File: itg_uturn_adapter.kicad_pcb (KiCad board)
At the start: 2 copper layers, 21.6 x 59.7 mm, 2 parts, among them J1 PinSocket_02x20, J2 BoxHeader_02x20

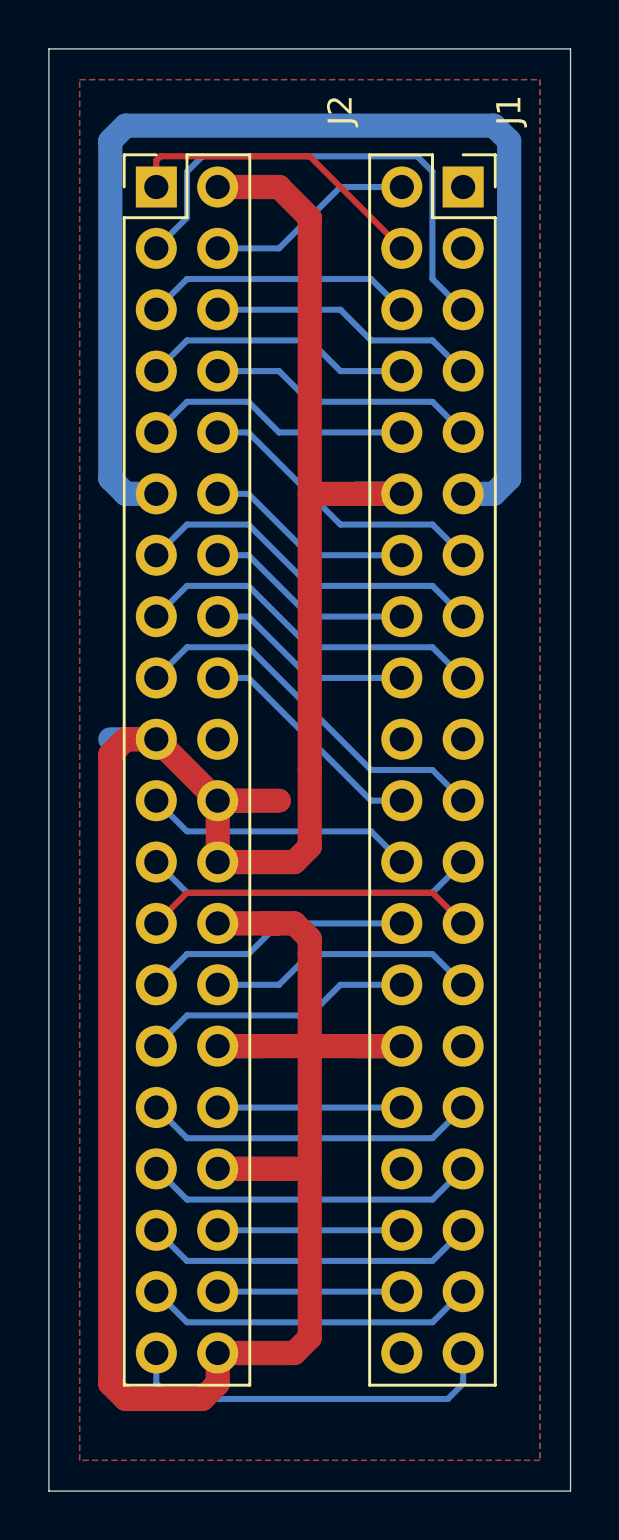
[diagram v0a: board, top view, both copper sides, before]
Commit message: modified external forms
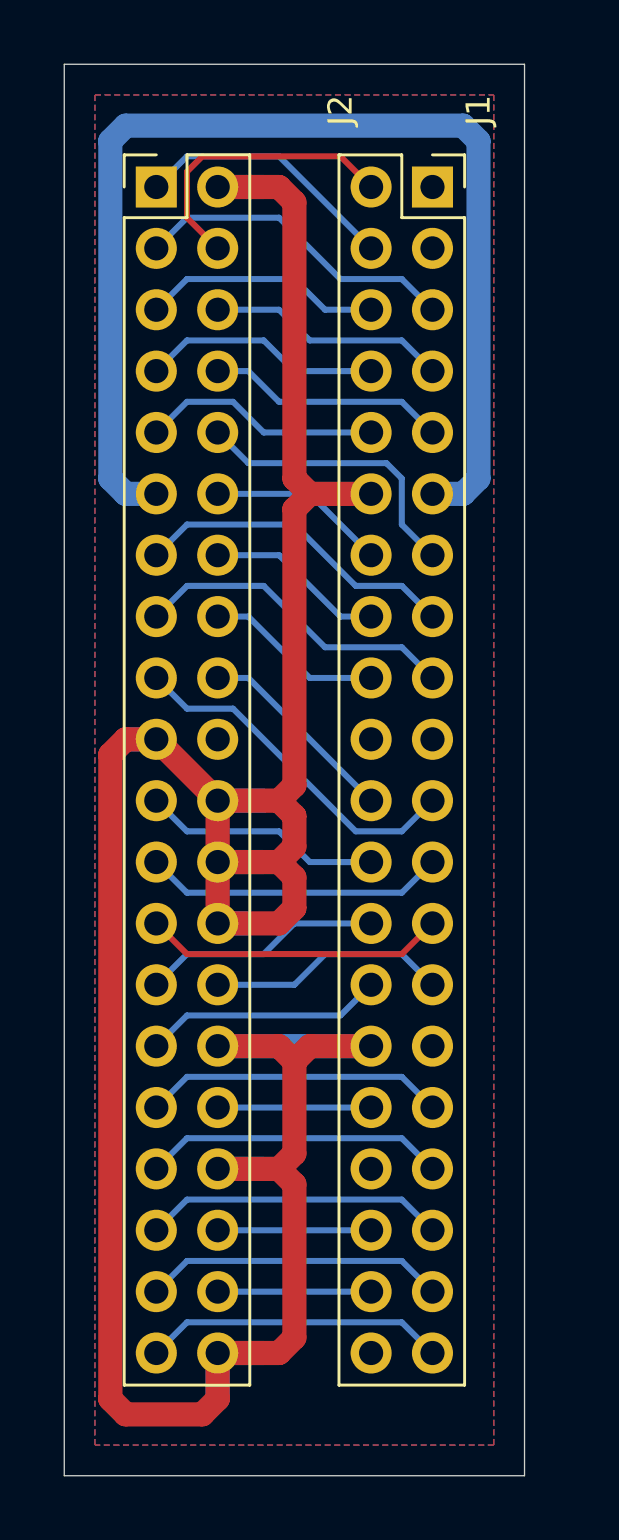
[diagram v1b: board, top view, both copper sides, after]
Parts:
- moved J1 1.27 mm to (102.9, 64.8)
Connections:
- net Net-(J1-Pad11) renamed +5V
- net Net-(J1-Pad12) renamed GND
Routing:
- net GND: track 183.7 -> 134.7 mm
- net Net-(J1-Pad5): track 20.6 -> 13.5 mm
- net Net-(J1-Pad2): track 8.67 -> 12.1 mm
- net Net-(J1-Pad39): track 15.8 -> 12.5 mm
- net Net-(J1-Pad4): track 12.9 -> 11.0 mm
- net Net-(J1-Pad37): track 13.8 -> 12.5 mm
- net Net-(J1-Pad33): track 13.8 -> 12.5 mm
- net Net-(J1-Pad21): track 15.9 -> 14.6 mm
- net Net-(J1-Pad7): track 11.2 -> 9.94 mm
- net Net-(J1-Pad10): track 11.2 -> 9.94 mm
- net Net-(J1-Pad35): track 13.8 -> 12.5 mm
- net Net-(J1-Pad25): track 13.8 -> 12.5 mm
- net Net-(J1-Pad23): track 13.8 -> 12.5 mm
- net Net-(J1-Pad9): track 11.2 -> 9.94 mm
- net Net-(J1-Pad8): track 11.2 -> 9.94 mm
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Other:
- board size 21.6 x 59.7 mm -> 19.1 x 58.4 mm
- rule trace_min: 0.2 -> 0.25

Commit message: add some vias to gnd
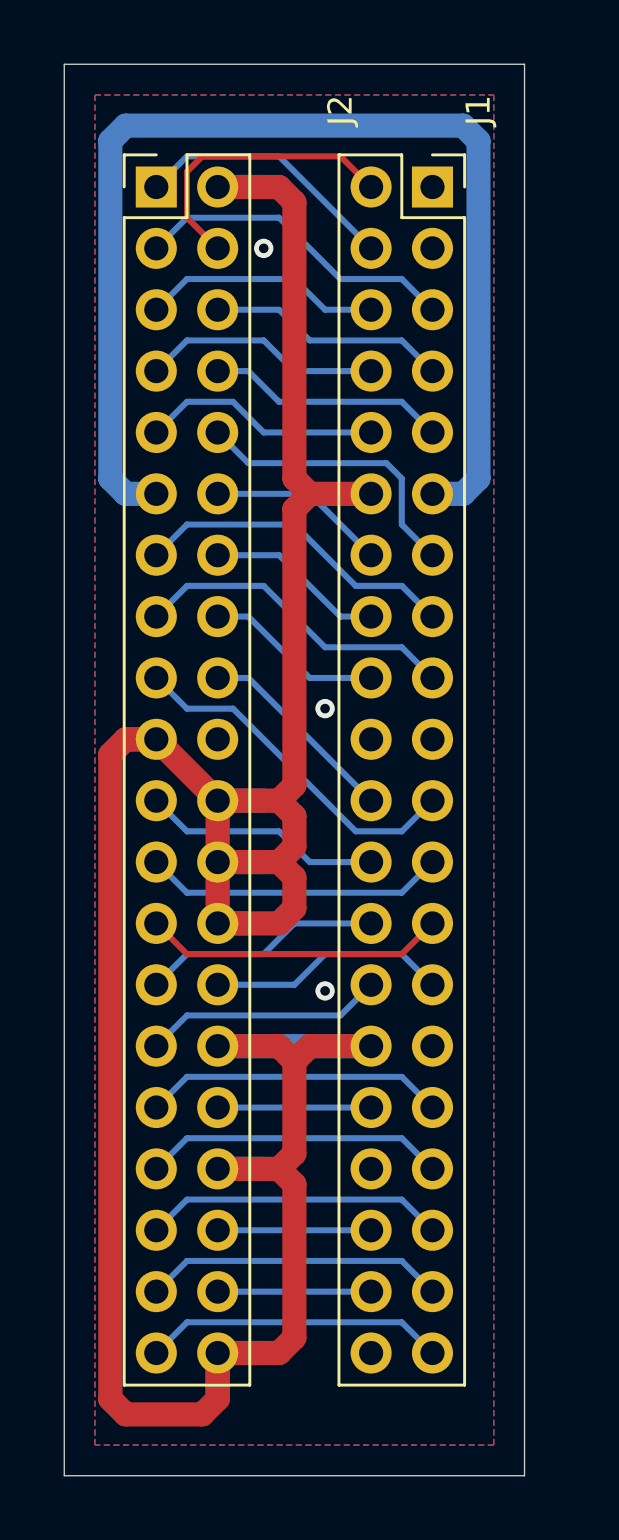
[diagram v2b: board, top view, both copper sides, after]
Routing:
- net GND: vias 0 -> 3
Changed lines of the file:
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@@
     (thickness 1.6)
     (drawings 12)
-    (tracks 160)
+    (tracks 163)
     (zones 0)
     (modules 2)
@@
   )
   (setup
-    (last_trace_width 0.25)
+    (last_trace_width 1)
     (user_trace_width 1)
     (trace_clearance 0.2)
@@
   (segment (start 97.79 100.33) (end 97.155 100.965) (width 1) (layer F.Cu) (net 40))
   (segment (start 93.98 100.33) (end 100.33 100.33) (width 1) (layer B.Cu) (net 40))
-  (segment (start 93.98 90.17) (end 91.44 87.63) (width 1) (layer F.Cu) (net 40))
   (segment (start 93.98 113.03) (end 93.98 114.935) (width 1) (layer B.Cu) (net 40))
   (segment (start 93.98 113.03) (end 95.885 113.03) (width 1) (layer B.Cu) (net 40))
@@
   (segment (start 93.98 64.77) (end 95.182081 64.77) (width 1) (layer B.Cu) (net 40))
   (segment (start 93.98 92.71) (end 95.885 92.71) (width 1) (layer B.Cu) (net 40))
+  (via (at 98.425 86.36) (size 0.8) (drill 0.4) (layers F.Cu B.Cu) (net 40))
+  (via (at 98.425 98.044) (size 0.8) (drill 0.4) (layers F.Cu B.Cu) (net 40))
+  (via (at 95.885 67.31) (size 0.8) (drill 0.4) (layers F.Cu B.Cu) (net 40))
+  (segment (start 93.98 90.17) (end 91.44 87.63) (width 1) (layer F.Cu) (net 40))
   (zone (net 40) (net_name GND) (layer F.Cu) (hatch edge 0.508)
     (connect_pads (clearance 0.508))
